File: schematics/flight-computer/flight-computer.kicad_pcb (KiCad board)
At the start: 4 copper layers, 80 x 80 mm, 113 parts, among them J101 BATT, J102 CHG, J103 Expansion Slot, J104 SWD, J105 BLACKBOX, J106 USB C, J107 GPS, J108 TELEM, J301 BMI-S-201, Q401 Si9933CDY, Q402 BSS138, U101 MAX14787E, U102 STM32F405RGT6, U201 TXS0108EPW, U202 ICM-20789, U203 MS5611-01BA, U301 Si4463, U302 MAX-M8Q, U401 BQ29200, U402 LTC4002-ES8, U403 MAX604, U404 MAX604, Y101 26M, Y301 LFTCXO068373

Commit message: Complete first draft
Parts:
- removed the C404 at (230.2, 152.0)
- removed the C405 at (232.7, 143.9)
- removed the C406 at (232.9, 152.0)
- removed the C408 at (223.1, 148.5)
- removed the D102 at (235.7, 159.3)
- removed D401, D402: B330, Strix:B330
- removed the J102 at (237.8, 158.3)
- removed L401: 6u8, Strix:L_Wuerth_HCI-7050
- removed Q401: Si9933CDY, Strix:Si9933CDY
- removed Q402: BSS138, Strix:BSS138
- removed the R401 at (231.6, 162.8)
- removed the R405 at (227.9, 146.5)
- removed the R406 at (227.4, 144.8)
- removed the R407 at (232.7, 146.3)
- removed R409: 50m, Strix:R_0402
- removed the U402 at (225.7, 152.0)
- added C203: 100n, Strix:C_0402, F.Cu at (231.8, 131.3)
- added R201: 200k, Strix:R_0402, F.Cu at (242.1, 139.8)
- added R202: 4k7, Strix:R_0402, F.Cu at (239.6, 138.7)
- added R203: 4k7, Strix:R_0402, F.Cu at (237.0, 138.7)
- added R204: 4k7, Strix:R_0402, F.Cu at (235.6, 131.7)
- added R404: 160, Strix:R_0402, F.Cu at (232.3, 150.9)
- added U204: PCA9306, Strix:PCA9306, F.Cu at (239.6, 134.3)
- R205: value 10k -> 4k7
- R403: value 261 -> 100
- U201: value TXS0108EPW -> NXB0108PW-Q100J; footprint Strix:TXS0108EPW -> Strix:NXB0108PW-Q100J
- U302: value MAX-M8Q -> MAX-M8; footprint Strix:MAX-M8Q -> Strix:MAX-M8
- moved C402 36.8 mm to (244.7, 164.3), turned to 180 degrees
- moved R406 33.0 mm to (233.0, 165.4), turned to 0 degrees
- moved C408 32.8 mm to (235.6, 164.3), turned to 180 degrees
- moved R407 30.9 mm to (233.0, 164.3), turned to 0 degrees
- moved C207 30.6 mm to (220.9, 149.6)
- moved U401 30.5 mm to (243.4, 160.0), turned to -90 degrees
- moved U203 30.4 mm to (218.3, 147.8)
- moved C401 25.6 mm to (244.7, 155.7), turned to 180 degrees
- moved C202 24.5 mm to (226.7, 140.1), turned to 0 degrees
- moved U403 24.0 mm to (234.3, 160.0), turned to -90 degrees
- moved C314 20.1 mm to (222.5, 127.8), turned to 0 degrees
- moved C208 19.0 mm to (242.1, 138.6)
- moved C407 18.9 mm to (235.6, 155.7), turned to 180 degrees
- moved U201 17.7 mm to (228.9, 136.0), turned to 180 degrees
- moved R402 16.3 mm to (229.2, 152.6)
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- renumbered C105 to C102, C107 to C103, C112 to C104, C102 to C105, C108 to C107, C109 to C108, C110 to C109, C111 to C110, C103 to C111, C104 to C112, C203 to C208, C310 to C303, C312 to C304, C313 to C305, C314 to C306, C311 to C307, C309 to C308, C304 to C309, C305 to C310, C306 to C311, C307 to C312, C308 to C313, C303 to C314, C409 to C401, C411 to C402, C401 to C403, C407 to C404, C402 to C405, C403 to C406, C410 to C407, C412 to C408, D103 to D101, D101 to D102, D113 to D103, D114 to D104, D110 to D105, D111 to D106, D112 to D107, D104 to D108, D105 to D109, D106 to D110, D107 to D111, D108 to D112, D109 to D113, J107 to J102, J108 to J103, J103 to J104, J106 to J105, J104 to J106, J105 to J107, L303 to L302, L305 to L303, L306 to L304, L307 to L305, L302 to L306, L304 to L307, R102 to R101, R104 to R102, R101 to R104, R408 to R401, R404 to R405, R411 to R406, R410 to R407, U102 to U101, U101 to U102, U403 to U401, U401 to U402, U404 to U403
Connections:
- C208 pad 2: 1v8 -> Net-(C208-Pad2)
- C403 pad 2: Net-(C401-Pad2) -> Net-(C403-Pad2)
- C405 pad 1: Net-(C401-Pad2) -> Net-(C403-Pad2)
- R205 pad 1: GND -> /Altimeter/SCL_1v8
- R403 pad 2: Net-(C401-Pad2) -> Net-(R403-Pad2)
- U101 pad 11: /CHG_SDN -> unconnected-(U101-Pad11)
- U201 pad 1: Net-(U201-Pad1) -> unconnected-(U201-Pad1)
- U201 pad 12: /SPI1_MOSI -> /IMU_INT
- U201 pad 13: /SPI1_SCLK -> unconnected-(U201-Pad13)
- U201 pad 15: /SPI1_MISO -> /SPI1_MOSI
- U201 pad 16: /IMU_INT -> /SPI1_MISO
- U201 pad 17: unconnected-(U201-Pad17) -> /SPI1_SCLK
- U201 pad 18: /I2C3_SCL -> unconnected-(U201-Pad18)
- U201 pad 20: /I2C3_SDA -> unconnected-(U201-Pad20)
- U201 pad 3: Net-(U201-Pad3) -> unconnected-(U201-Pad3)
- U201 pad 4: Net-(U201-Pad4) -> Net-(U202-Pad23)
- U201 pad 5: Net-(U201-Pad5) -> Net-(U202-Pad9)
- U201 pad 6: unconnected-(U201-Pad6) -> Net-(U202-Pad24)
- U201 pad 7: Net-(U201-Pad7) -> Net-(U202-Pad22)
- U201 pad 8: Net-(U201-Pad8) -> unconnected-(U201-Pad8)
- U201 pad 9: Net-(U201-Pad9) -> Net-(U202-Pad12)
- U202 pad 12: Net-(U201-Pad1) -> Net-(U202-Pad12)
- U202 pad 22: Net-(U201-Pad9) -> Net-(U202-Pad22)
- U202 pad 23: Net-(U201-Pad8) -> Net-(U202-Pad23)
- U202 pad 24: Net-(U201-Pad7) -> Net-(U202-Pad24)
- U202 pad 6: Net-(U201-Pad5) -> /Altimeter/SDA_1v8
- U202 pad 7: Net-(U201-Pad4) -> /Altimeter/SCL_1v8
- U202 pad 9: Net-(U201-Pad3) -> Net-(U202-Pad9)
- U402 pad 2: Net-(C401-Pad2) -> Net-(C403-Pad2)
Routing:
- net /BARO_~{CS}: track 58.7 -> 25.5 mm
- net /CHG_SDN: track 30.3 -> 0.00 mm, vias 2 -> 0
- net /I2C3_SCL: track 34.0 -> 56.7 mm
- net /I2C3_SDA: track 32.7 -> 55.1 mm
- net /PSU/~{CHRG}: track 20.3 -> 0.00 mm, vias 3 -> 0
- net /RADIO_~{CS}: track 21.6 -> 40.9 mm, vias 0 -> 2
- net /SPI2_MOSI: track 24.5 -> 43.1 mm, vias 0 -> 2
- net /SPI1_MISO: track 63.1 -> 44.7 mm
- net Net-(U202-Pad9): track 0.00 -> 18.3 mm, vias 0 -> 2
- net /PSU/BATT_MON: track 17.7 -> 0.00 mm, vias 1 -> 0
- net /SPI2_MISO: track 23.7 -> 40.6 mm, vias 0 -> 2
- net /IMU_INT: track 56.4 -> 39.7 mm, vias 2 -> 0
- net GND: track 105.2 -> 88.6 mm, vias 52 -> 129
- net /SPI1_MOSI: track 66.5 -> 50.3 mm
- net /SPI1_SCLK: track 66.6 -> 50.5 mm, vias 2 -> 0
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- added copper zone on F.Cu, net /PSU/BATT_MON
- removed copper zone on F.Cu, net /CHG_SDN
- removed copper zone on F.Cu, net /PSU/CHG+
- removed copper zone on F.Cu, net /PSU/COMP
- removed copper zone on F.Cu, net /PSU/SENSE
- removed copper zone on F.Cu, net /PSU/VCC_CHG
- removed copper zone on F.Cu, net /PSU/V_SW
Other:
- outline, holes or cut-outs redrawn
- board text added: "CU Spaceflight"
- board text added: "Jan. 2022"
- board text added: "Made in Cambridge, UK Board drawn by H. Franks"
- board text removed: "2022 CU Spaceflight"

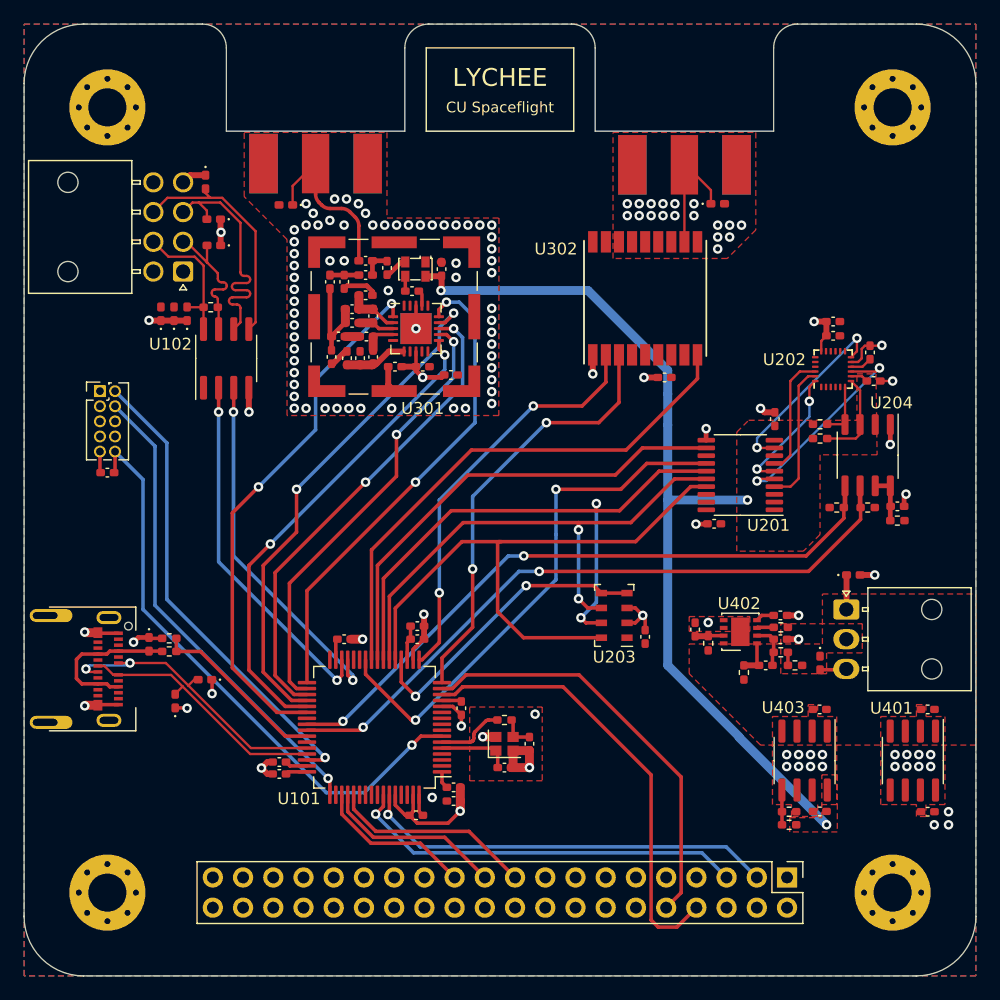
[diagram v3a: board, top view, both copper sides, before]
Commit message: Add test points
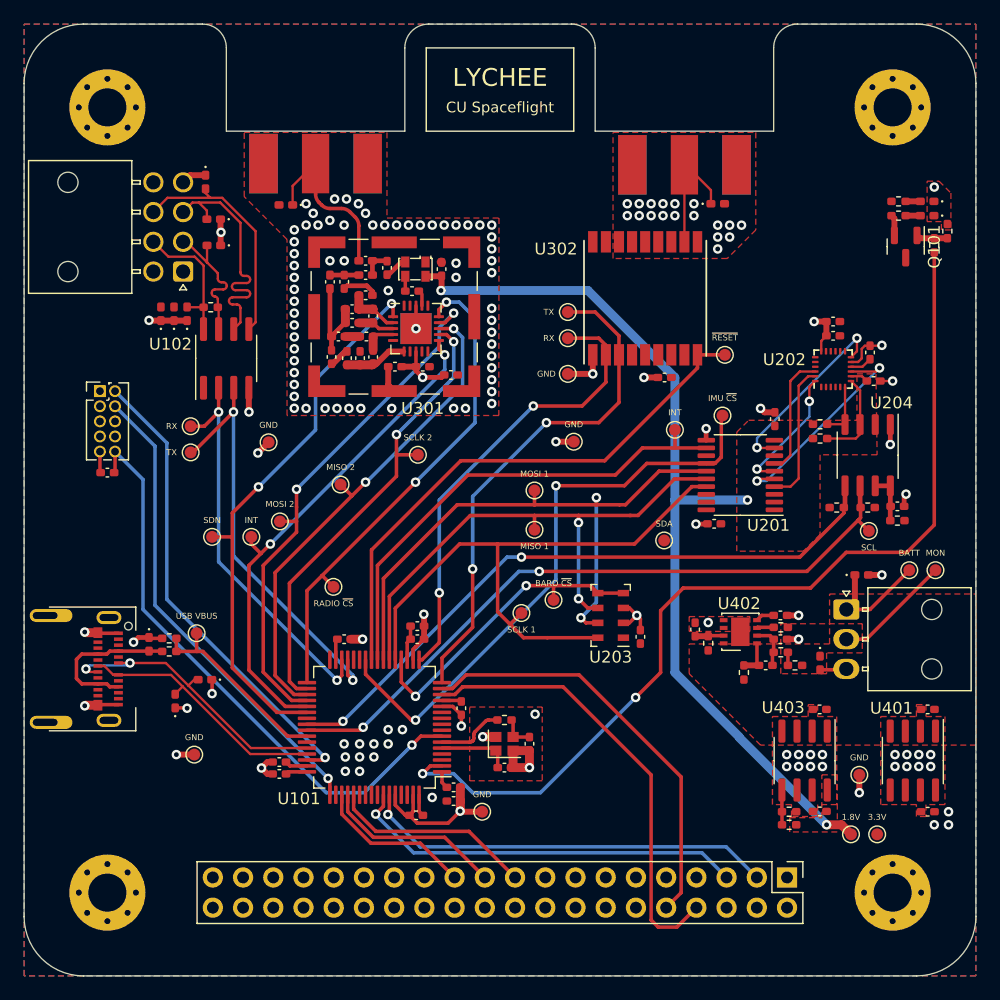
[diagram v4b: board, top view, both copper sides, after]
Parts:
- added 1.8V: TestPoint, Strix:TestPoint, F.Cu at (238.2, 166.2)
- added 3.3V: TestPoint, Strix:TestPoint, F.Cu at (240.4, 166.2)
- added BARO ~{CS}: TestPoint, Strix:TestPoint, F.Cu at (213.2, 146.5)
- added BATT: TestPoint, Strix:TestPoint, F.Cu at (243.1, 144.0)
- added D105: RED, Strix:LED_0402, F.Cu at (244.6, 113.0)
- added D106: YLW, Strix:LED_0402, F.Cu at (244.6, 114.2)
- added GND: TestPoint, Strix:TestPoint, F.Cu at (183.0, 159.5)
- added GND: TestPoint, Strix:TestPoint, F.Cu at (238.9, 161.2)
- added GND: TestPoint, Strix:TestPoint, F.Cu at (189.2, 133.2)
- added GND: TestPoint, Strix:TestPoint, F.Cu at (214.4, 127.5)
- added GND: TestPoint, Strix:TestPoint, F.Cu at (207.2, 164.3)
- added GND: TestPoint, Strix:TestPoint, F.Cu at (214.9, 133.2)
- added IMU ~{CS}: TestPoint, Strix:TestPoint, F.Cu at (227.4, 131.0)
- added INT: TestPoint, Strix:TestPoint, F.Cu at (187.8, 141.2)
- added INT: TestPoint, Strix:TestPoint, F.Cu at (223.4, 132.2)
- added MISO 1: TestPoint, Strix:TestPoint, F.Cu at (211.6, 140.6)
- added MISO 2: TestPoint, Strix:TestPoint, F.Cu at (195.3, 136.8)
- added MON: TestPoint, Strix:TestPoint, F.Cu at (245.3, 144.0)
- added MOSI 1: TestPoint, Strix:TestPoint, F.Cu at (211.6, 137.3)
- added MOSI 2: TestPoint, Strix:TestPoint, F.Cu at (190.2, 139.9)
- added Q101: BSS138, Strix:BSS138, F.Cu at (242.8, 116.8)
- added R101: 100, Strix:R_0402, F.Cu at (245.2, 116.7)
- added R102: 50, Strix:R_0402, F.Cu at (242.2, 113.0)
- added R103: 50, Strix:R_0402, F.Cu at (242.2, 114.2)
- added R104: 110k, Strix:R_0402, F.Cu at (246.3, 115.5)
- added RADIO ~{CS}: TestPoint, Strix:TestPoint, F.Cu at (194.7, 145.4)
- added RX: TestPoint, Strix:TestPoint, F.Cu at (182.7, 131.9)
- added RX: TestPoint, Strix:TestPoint, F.Cu at (214.4, 124.5)
- added SCL: TestPoint, Strix:TestPoint, F.Cu at (239.7, 140.7)
- added SCLK 1: TestPoint, Strix:TestPoint, F.Cu at (210.5, 147.6)
- added SCLK 2: TestPoint, Strix:TestPoint, F.Cu at (201.8, 134.3)
- added SDA: TestPoint, Strix:TestPoint, F.Cu at (222.5, 141.5)
- added SDN: TestPoint, Strix:TestPoint, F.Cu at (184.5, 141.2)
- added TX: TestPoint, Strix:TestPoint, F.Cu at (214.4, 122.3)
- added TX: TestPoint, Strix:TestPoint, F.Cu at (182.7, 134.1)
- added USB VBUS: TestPoint, Strix:TestPoint, F.Cu at (183.2, 149.3)
- added ~{RESET}: TestPoint, Strix:TestPoint, F.Cu at (227.6, 125.9)
- moved D101 0.70 mm to (239.1, 144.4)
- moved C207 0.40 mm to (220.5, 149.6)
- moved U203 0.30 mm to (218.0, 147.8)
- renumbered D105 to D107, D106 to D108, D107 to D109, D108 to D110, D109 to D111, D110 to D112, D111 to D113, D112 to D114, D113 to D115, R101 to R105, R102 to R106, R103 to R107, R104 to R108
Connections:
- net /PSU/BATT_MON renamed /BATT_MON
- U101 pad 2: unconnected-(U101-Pad2) -> /LED
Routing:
- net /LED: track 0.00 -> 80.8 mm, vias 0 -> 2
- net /BATT_MON: track 0.00 -> 9.89 mm
- net GND: track 88.6 -> 97.9 mm, vias 129 -> 134
- net VBATT: track 2.91 -> 9.85 mm
- net /USART2_TX: track 36.3 -> 43.0 mm
- net /IMU_~{CS}: track 44.8 -> 50.0 mm
- net /USART3_TX: track 30.6 -> 35.7 mm
- net /USART2_RX: track 34.7 -> 38.9 mm
- net /USART3_RX: track 30.6 -> 33.4 mm
- net Net-(Q101-Pad1): track 0.00 -> 2.65 mm
- net /SPI2_SCLK: track 37.5 -> 39.3 mm
- net 1v8: track 76.3 -> 78.1 mm
- net /GPS_~{RESET}: track 44.6 -> 46.4 mm
- net Net-(Q101-Pad2): track 0.00 -> 1.77 mm
- net /RADIO_~{INT}: track 40.9 -> 42.6 mm
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
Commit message: Clean up silkscreen
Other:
- board text added: "Made in Cambridge, UK Designed by H. Franks"
- board text removed: "Made in Cambridge, UK Board drawn by H. Franks"
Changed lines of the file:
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@@
     (fp_line (start -0.167621 -0.38) (end 0.167621 -0.38) (layer "F.SilkS") (width 0.12))
     (fp_line (start -0.167621 0.38) (end 0.167621 0.38) (layer "F.SilkS") (width 0.12))
-    (fp_line (start -1.1 -0.47) (end 1.1 -0.47) (layer "F.CrtYd") (width 0.05))
     (fp_line (start 1.1 0.47) (end -1.1 0.47) (layer "F.CrtYd") (width 0.05))
+    (fp_line (start -1.1 -0.47) (end 1.1 -0.47) (layer "F.CrtYd") (width 0.05))
     (fp_line (start -1.1 0.47) (end -1.1 -0.47) (layer "F.CrtYd") (width 0.05))
     (fp_line (start 1.1 -0.47) (end 1.1 0.47) (layer "F.CrtYd") (width 0.05))
@@
     (fp_line (start -0.167621 0.38) (end 0.167621 0.38) (layer "F.SilkS") (width 0.12))
     (fp_line (start -0.167621 -0.38) (end 0.167621 -0.38) (layer "F.SilkS") (width 0.12))
-    (fp_line (start 1.1 -0.47) (end 1.1 0.47) (layer "F.CrtYd") (width 0.05))
-    (fp_line (start -1.1 -0.47) (end 1.1 -0.47) (layer "F.CrtYd") (width 0.05))
-    (fp_line (start 1.1 0.47) (end -1.1 0.47) (layer "F.CrtYd") (width 0.05))
     (fp_line (start -1.1 0.47) (end -1.1 -0.47) (layer "F.CrtYd") (width 0.05))
-    (fp_line (start 0.525 -0.27) (end 0.525 0.27) (layer "F.Fab") (width 0.1))
+    (fp_line (start 1.1 0.47) (end -1.1 0.47) (layer "F.CrtYd") (width 0.05))
+    (fp_line (start -1.1 -0.47) (end 1.1 -0.47) (layer "F.CrtYd") (width 0.05))
+    (fp_line (start 1.1 -0.47) (end 1.1 0.47) (layer "F.CrtYd") (width 0.05))
     (fp_line (start -0.525 0.27) (end -0.525 -0.27) (layer "F.Fab") (width 0.1))
     (fp_line (start -0.525 -0.27) (end 0.525 -0.27) (layer "F.Fab") (width 0.1))
     (fp_line (start 0.525 0.27) (end -0.525 0.27) (layer "F.Fab") (width 0.1))
+    (fp_line (start 0.525 -0.27) (end 0.525 0.27) (layer "F.Fab") (width 0.1))
     (pad "1" smd roundrect (at -0.5975 0 270) (size 0.715 0.64) (layers "F.Cu" "F.Paste" "F.Mask") (roundrect_rratio 0.25)
       (net 2 "GND") (pintype "passive"))
@@
     (fp_line (start -1.1 -0.47) (end 1.1 -0.47) (layer "F.CrtYd") (width 0.05))
     (fp_line (start 0.525 -0.27) (end 0.525 0.27) (layer "F.Fab") (width 0.1))
+    (fp_line (start 0.525 0.27) (end -0.525 0.27) (layer "F.Fab") (width 0.1))
     (fp_line (start -0.525 -0.27) (end 0.525 -0.27) (layer "F.Fab") (width 0.1))
     (fp_line (start -0.525 0.27) (end -0.525 -0.27) (layer "F.Fab") (width 0.1))
-    (fp_line (start 0.525 0.27) (end -0.525 0.27) (layer "F.Fab") (width 0.1))
     (pad "1" smd roundrect (at -0.5975 0 90) (size 0.715 0.64) (layers "F.Cu" "F.Paste" "F.Mask") (roundrect_rratio 0.25)
       (net 153 "/LED") (pintype "passive"))
@@
     (fp_line (start 1.1 0.47) (end -1.1 0.47) (layer "F.CrtYd") (width 0.05))
     (fp_line (start -1.1 0.47) (end -1.1 -0.47) (layer "F.CrtYd") (width 0.05))
-    (fp_line (start -1.1 -0.47) (end 1.1 -0.47) (layer "F.CrtYd") (width 0.05))
     (fp_line (start 1.1 -0.47) (end 1.1 0.47) (layer "F.CrtYd") (width 0.05))
+    (fp_line (start -1.1 -0.47) (end 1.1 -0.47) (layer "F.CrtYd") (width 0.05))
+    (fp_line (start 0.525 -0.27) (end 0.525 0.27) (layer "F.Fab") (width 0.1))
+    (fp_line (start -0.525 0.27) (end -0.525 -0.27) (layer "F.Fab") (width 0.1))
     (fp_line (start 0.525 0.27) (end -0.525 0.27) (layer "F.Fab") (width 0.1))
     (fp_line (start -0.525 -0.27) (end 0.525 -0.27) (layer "F.Fab") (width 0.1))
-    (fp_line (start -0.525 0.27) (end -0.525 -0.27) (layer "F.Fab") (width 0.1))
-    (fp_line (start 0.525 -0.27) (end 0.525 0.27) (layer "F.Fab") (width 0.1))
     (pad "1" smd roundrect (at -0.5975 0) (size 0.715 0.64) (layers "F.Cu" "F.Paste" "F.Mask") (roundrect_rratio 0.25)
       (net 101 "/I2C3_SCL") (pintype "passive"))
@@
     (fp_line (start -1.1 -0.47) (end 1.1 -0.47) (layer "F.CrtYd") (width 0.05))
     (fp_line (start 1.1 0.47) (end -1.1 0.47) (layer "F.CrtYd") (width 0.05))
-    (fp_line (start -0.5 -0.25) (end 0.5 -0.25) (layer "F.Fab") (width 0.1))
+    (fp_line (start 0.5 0.25) (end -0.5 0.25) (layer "F.Fab") (width 0.1))
     (fp_line (start -0.4 0.25) (end -0.4 -0.25) (layer "F.Fab") (width 0.1))
     (fp_line (start -0.3 0.25) (end -0.3 -0.25) (layer "F.Fab") (width 0.1))
     (fp_line (start -0.5 0.25) (end -0.5 -0.25) (layer "F.Fab") (width 0.1))
-    (fp_line (start 0.5 0.25) (end -0.5 0.25) (layer "F.Fab") (width 0.1))
     (fp_line (start 0.5 -0.25) (end 0.5 0.25) (layer "F.Fab") (width 0.1))
+    (fp_line (start -0.5 -0.25) (end 0.5 -0.25) (layer "F.Fab") (width 0.1))
     (pad "1" smd roundrect (at -0.5725 0 180) (size 0.765 0.64) (layers "F.Cu" "F.Paste" "F.Mask") (roundrect_rratio 0.25)
       (net 2 "GND") (pintype "passive"))
@@
     (fp_line (start -1.1 -0.47) (end 1.1 -0.47) (layer "F.CrtYd") (width 0.05))
     (fp_line (start -0.525 0.27) (end -0.525 -0.27) (layer "F.Fab") (width 0.1))
-    (fp_line (start 0.525 -0.27) (end 0.525 0.27) (layer "F.Fab") (width 0.1))
-    (fp_line (start -0.525 -0.27) (end 0.525 -0.27) (layer "F.Fab") (width 0.1))
     (fp_line (start 0.525 0.27) (end -0.525 0.27) (layer "F.Fab") (width 0.1))
+    (fp_line (start -0.525 -0.27) (end 0.525 -0.27) (layer "F.Fab") (width 0.1))
+    (fp_line (start 0.525 -0.27) (end 0.525 0.27) (layer "F.Fab") (width 0.1))
     (pad "1" smd roundrect (at -0.5975 0 180) (size 0.715 0.64) (layers "F.Cu" "F.Paste" "F.Mask") (roundrect_rratio 0.25)
       (net 59 "Net-(D105-Pad2)") (pintype "passive"))
@@
     (fp_line (start -0.167621 0.38) (end 0.167621 0.38) (layer "F.SilkS") (width 0.12))
     (fp_line (start -0.167621 -0.38) (end 0.167621 -0.38) (layer "F.SilkS") (width 0.12))
-    (fp_line (start -1.1 -0.47) (end 1.1 -0.47) (layer "F.CrtYd") (width 0.05))
     (fp_line (start 1.1 -0.47) (end 1.1 0.47) (layer "F.CrtYd") (width 0.05))
     (fp_line (start -1.1 0.47) (end -1.1 -0.47) (layer "F.CrtYd") (width 0.05))
+    (fp_line (start -1.1 -0.47) (end 1.1 -0.47) (layer "F.CrtYd") (width 0.05))
     (fp_line (start 1.1 0.47) (end -1.1 0.47) (layer "F.CrtYd") (width 0.05))
     (fp_line (start -0.525 -0.27) (end 0.525 -0.27) (layer "F.Fab") (width 0.1))
-    (fp_line (start 0.525 -0.27) (end 0.525 0.27) (layer "F.Fab") (width 0.1))
-    (fp_line (start -0.525 0.27) (end -0.525 -0.27) (layer "F.Fab") (width 0.1))
     (fp_line (start 0.525 0.27) (end -0.525 0.27) (layer "F.Fab") (width 0.1))
+    (fp_line (start -0.525 0.27) (end -0.525 -0.27) (layer "F.Fab") (width 0.1))
+    (fp_line (start 0.525 -0.27) (end 0.525 0.27) (layer "F.Fab") (width 0.1))
     (pad "1" smd roundrect (at -0.5975 0) (size 0.715 0.64) (layers "F.Cu" "F.Paste" "F.Mask") (roundrect_rratio 0.25)
       (net 131 "Net-(C208-Pad2)") (pintype "passive"))
@@
   (gr_line (start 200.7 100.1) (end 200.7 107.1) (layer "Edge.Cuts") (width 0.05))
   (gr_line (start 233.7 98.1) (end 243.7 98.1) (layer "Edge.Cuts") (width 0.05))
-  (gr_text "Made in Cambridge, UK\n\nBoard drawn by H. Franks" (at 208.8 102.7) (layer "B.SilkS")
+  (gr_text "Made in Cambridge, UK\n\nDesigned by H. Franks" (at 208.7 102.7) (layer "B.SilkS")
     (effects (font (size 0.6 0.6) (thickness 0.1)) (justify mirror))
   )
-  (gr_text "Jan. 2022" (at 208.6 104.9) (layer "B.SilkS")
+  (gr_text "Jan. 2022" (at 208.7 104.9) (layer "B.SilkS")
     (effects (font (size 0.6 0.6) (thickness 0.1)) (justify mirror))
   )
@@
   (via (at 185.05 130.7) (size 0.8) (drill 0.4) (layers "F.Cu" "B.Cu") (net 24))
   (via (at 195 153.25) (size 0.8) (drill 0.4) (layers "F.Cu" "B.Cu") (net 24))
-  (segment (start 185.05 130.7) (end 185.05 143.3) (width 0.3) (layer "B.Cu") (net 24))
   (segment (start 185.05 143.3) (end 195 153.25) (width 0.3) (layer "B.Cu") (net 24))
+  (segment (start 185.05 130.7) (end 185.05 143.3) (width 0.3) (layer "B.Cu") (net 24))
   (segment (start 196.327943 153.25) (end 195.9 152.822057) (width 0.3) (layer "F.Cu") (net 25))
   (segment (start 182.9 134.1) (end 186.3 130.7) (width 0.3) (layer "F.Cu") (net 25))

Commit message: Final changes for manufacture
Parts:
- added G***: LOGO, Strix:CUSF_Logo, B.Cu at (218.6, 157.4)
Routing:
- net /BATT_MON: track 9.89 -> 12.7 mm, vias 0 -> 1
- net /I2C3_SDA: track 54.8 -> 56.2 mm
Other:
- rule pad_to_mask_clearance: 0.05 -> 0
